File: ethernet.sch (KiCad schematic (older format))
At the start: 49 parts, among them U6 KSZ9031RNXCA, Y1 ABM8G-25.000MHZ-18-D2Y-T

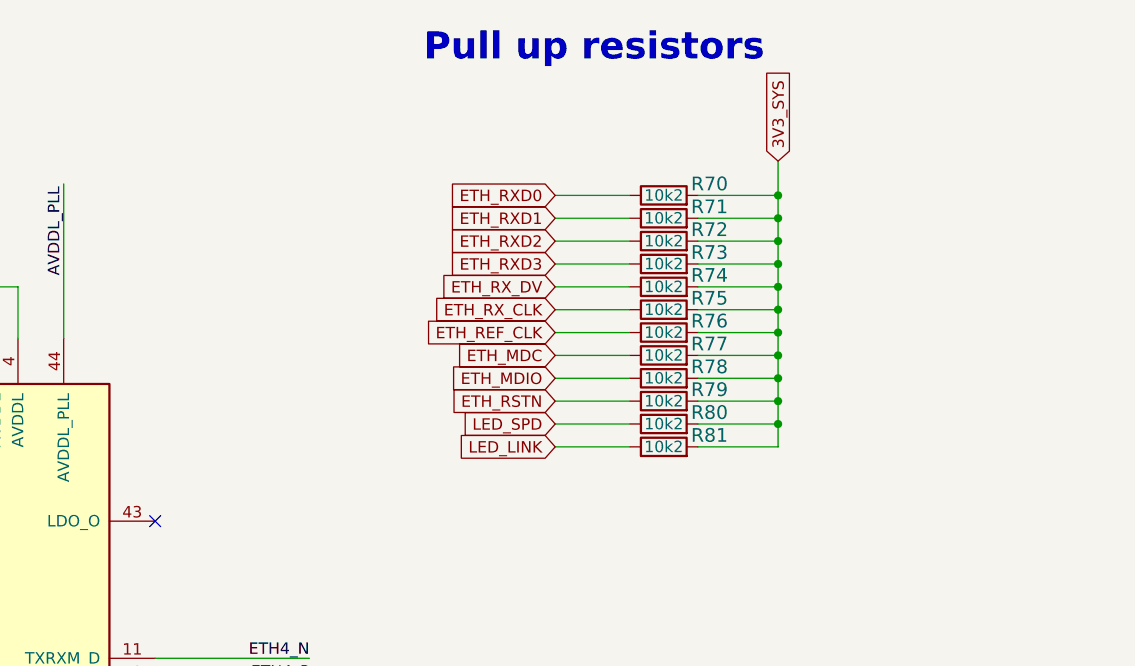
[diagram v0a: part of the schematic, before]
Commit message: Add bootstrap pull down resistors
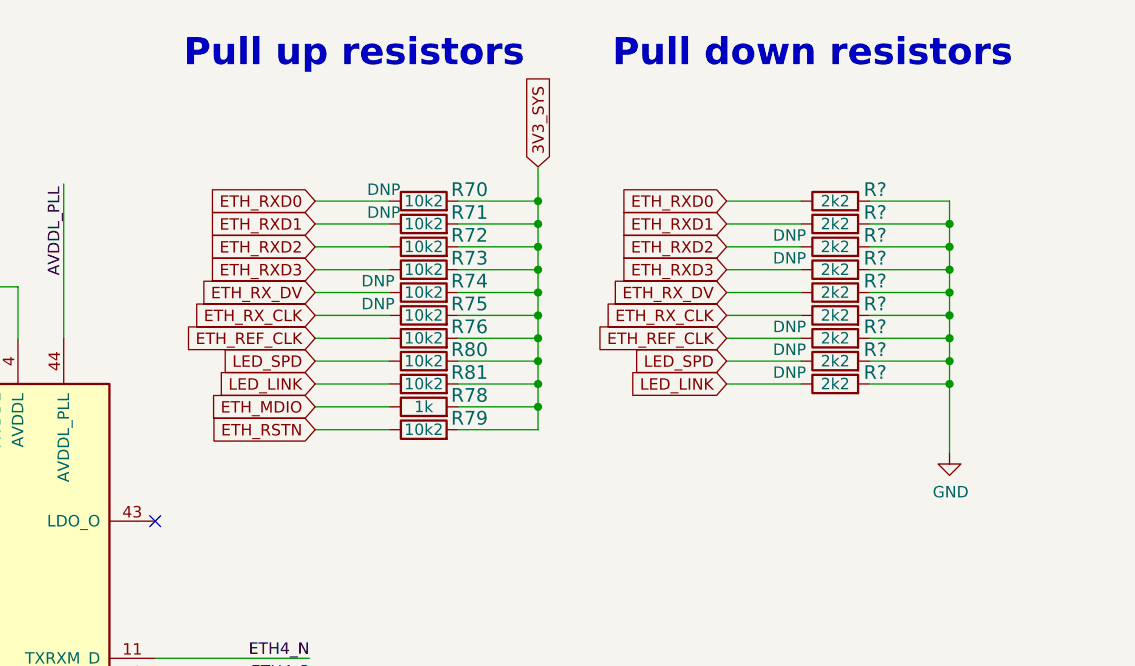
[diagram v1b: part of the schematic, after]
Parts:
- removed R77, R78: R_10k2_0402, lpddr4-test-board-footprints:0402-res, symbol lpddr4-test-board:R_10k2_0402
- added R78: R_1k_0402, antmicro-footprints:0402-res, symbol antmicroResistors0402:R_1k_0402
- added R? (x9): R_2k2_0402, antmicro-footprints:0402-res, symbol antmicroResistors0402:R_2k2_0402
- R70, R71, R74, R75: DNP (none) -> DNP
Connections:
- net 3V3_SYS: now also R78.2
- net ETH_MDIO: now also R78.1
- net ETH_REF_CLK: now also R?.1
- net ETH_RXD0: now also R?.1
- net ETH_RXD1: now also R?.1
- net ETH_RXD2: now also R?.1
- net ETH_RXD3: now also R?.1
- net ETH_RX_CLK: now also R?.1
- net ETH_RX_DV: now also R?.1
- net GND: now also R?.2, R?.2, R?.2, R?.2, R?.2, R?.2, R?.2, R?.2, R?.2
- net LED_LINK: now also R?.1
- net LED_SPD: now also R?.1
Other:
- note added: "Pull down resistors"
- moved on the sheet: R70, R71, R72, R73, R74, R75, R76, R79, R80, R81

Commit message: Bump release to 1.0.5
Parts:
- gave numbers to parts that had none: 9
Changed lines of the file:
@@
 	15300 2050 15650 2050
 $Comp
-L antmicroResistors0402:R_2k2_0402 R?
+L antmicroResistors0402:R_2k2_0402 R77
 U 1 1 6075D996
 P 15150 1750
-F 0 "R?" H 15325 1800 60  0000 C CNN
+F 0 "R77" H 15325 1800 60  0000 C CNN
 F 1 "R_2k2_0402" H 15150 1600 60  0001 C CNN
 F 2 "antmicro-footprints:0402-res" H 15350 1950 60  0001 L CNN
@@
 $EndComp
 $Comp
-L antmicroResistors0402:R_2k2_0402 R?
+L antmicroResistors0402:R_2k2_0402 R89
 U 1 1 60761864
 P 15150 1850
-F 0 "R?" H 15325 1900 60  0000 C CNN
+F 0 "R89" H 15325 1900 60  0000 C CNN
 F 1 "R_2k2_0402" H 15150 1700 60  0001 C CNN
 F 2 "antmicro-footprints:0402-res" H 15350 2050 60  0001 L CNN
@@
 $EndComp
 $Comp
-L antmicroResistors0402:R_2k2_0402 R?
+L antmicroResistors0402:R_2k2_0402 R90
 U 1 1 60761EC5
 P 15150 1950
-F 0 "R?" H 15325 2000 60  0000 C CNN
+F 0 "R90" H 15325 2000 60  0000 C CNN
 F 1 "R_2k2_0402" H 15150 1800 60  0001 C CNN
 F 2 "antmicro-footprints:0402-res" H 15350 2150 60  0001 L CNN
@@
 $EndComp
 $Comp
-L antmicroResistors0402:R_2k2_0402 R?
+L antmicroResistors0402:R_2k2_0402 R91
 U 1 1 607623D6
 P 15150 2050
-F 0 "R?" H 15325 2100 60  0000 C CNN
+F 0 "R91" H 15325 2100 60  0000 C CNN
 F 1 "R_2k2_0402" H 15150 1900 60  0001 C CNN
 F 2 "antmicro-footprints:0402-res" H 15350 2250 60  0001 L CNN
@@
 $EndComp
 $Comp
-L antmicroResistors0402:R_2k2_0402 R?
+L antmicroResistors0402:R_2k2_0402 R92
 U 1 1 6076538B
 P 15150 2150
-F 0 "R?" H 15325 2200 60  0000 C CNN
+F 0 "R92" H 15325 2200 60  0000 C CNN
 F 1 "R_2k2_0402" H 15150 2000 60  0001 C CNN
 F 2 "antmicro-footprints:0402-res" H 15350 2350 60  0001 L CNN
@@
 $EndComp
 $Comp
-L antmicroResistors0402:R_2k2_0402 R?
+L antmicroResistors0402:R_2k2_0402 R93
 U 1 1 607655D6
 P 15150 2250
-F 0 "R?" H 15325 2300 60  0000 C CNN
+F 0 "R93" H 15325 2300 60  0000 C CNN
 F 1 "R_2k2_0402" H 15150 2100 60  0001 C CNN
 F 2 "antmicro-footprints:0402-res" H 15350 2450 60  0001 L CNN
@@
 $EndComp
 $Comp
-L antmicroResistors0402:R_2k2_0402 R?
+L antmicroResistors0402:R_2k2_0402 R95
 U 1 1 6077DB28
 P 15150 2450
-F 0 "R?" H 15325 2500 60  0000 C CNN
+F 0 "R95" H 15325 2500 60  0000 C CNN
 F 1 "R_2k2_0402" H 15150 2300 60  0001 C CNN
 F 2 "antmicro-footprints:0402-res" H 15350 2650 60  0001 L CNN
@@
 $EndComp
 $Comp
-L antmicroResistors0402:R_2k2_0402 R?
+L antmicroResistors0402:R_2k2_0402 R96
 U 1 1 6077E011
 P 15150 2550
-F 0 "R?" H 15325 2600 60  0000 C CNN
+F 0 "R96" H 15325 2600 60  0000 C CNN
 F 1 "R_2k2_0402" H 15150 2400 60  0001 C CNN
 F 2 "antmicro-footprints:0402-res" H 15350 2750 60  0001 L CNN
@@
 	15650 2550 15650 2850
 $Comp
-L lpddr4-test-board:GND #PWR?
+L lpddr4-test-board:GND #PWR0129
 U 1 1 607C5C08
 P 15650 2850
-F 0 "#PWR?" H 15650 2600 50  0001 C CNN
+F 0 "#PWR0129" H 15650 2600 50  0001 C CNN
 F 1 "GND" H 15655 2677 50  0000 C CNN
 F 2 "" H 15650 2850 50  0001 C CNN
@@
 $EndComp
 $Comp
-L antmicroResistors0402:R_2k2_0402 R?
+L antmicroResistors0402:R_2k2_0402 R94
 U 1 1 607AC011
 P 15150 2350
-F 0 "R?" H 15325 2400 60  0000 C CNN
+F 0 "R94" H 15325 2400 60  0000 C CNN
 F 1 "R_2k2_0402" H 15150 2200 60  0001 C CNN
 F 2 "antmicro-footprints:0402-res" H 15350 2550 60  0001 L CNN

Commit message: Update component libraries
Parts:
- C122, C126, C130: footprint antmicro-footprints:0402-cap -> lpddr4-test-board-footprints:0402-cap; symbol antmicroCapacitors0402:C_470n_0402 -> lpddr4-test-board:C_470n_0402
- C135, C138, C141, C142: footprint antmicro-footprints:0402-cap -> lpddr4-test-board-footprints:0402-cap; symbol antmicroCapacitors0402:C_10n_0402 -> lpddr4-test-board:C_10n_0402
- C140: footprint antmicro-footprints:0402-cap -> lpddr4-test-board-footprints:0402-cap; symbol antmicroCapacitors0402:C_4u7_0402 -> lpddr4-test-board:C_4u7_0402
- C147, C148: footprint antmicro-footprints:0402-cap -> lpddr4-test-board-footprints:0402-cap; symbol antmicroCapacitors0402:C_22p_0402 -> lpddr4-test-board:C_22p_0402
- FB1, FB2, FB3, FB7: footprint antmicro-footprints:0603-res -> lpddr4-test-board-footprints:0603-res; symbol antmicroFerriteBeadsandChips:BLM18PG121SN1D -> lpddr4-test-board:BLM18PG121SN1D
- J?1: footprint antmicro-footprints:7499111121A -> lpddr4-test-board-footprints:7499111121A; symbol antmicroModularConnectorsJacksWithMagnetics:WE-RJ45_7499111121A -> lpddr4-test-board:WE-RJ45_7499111121A
- R68: footprint antmicro-footprints:0402-res -> lpddr4-test-board-footprints:0402-res; symbol antmicroResistors0402:R_12k1_0402 -> lpddr4-test-board:R_12k1_0402
- R69: footprint antmicro-footprints:0402-res -> lpddr4-test-board-footprints:0402-res; symbol antmicroResistors0402:R_1M8_0402 -> lpddr4-test-board:R_1M8_0402
- R77, R89, R90, R91, R92, R93, R94, R95, R96: footprint antmicro-footprints:0402-res -> lpddr4-test-board-footprints:0402-res; symbol antmicroResistors0402:R_2k2_0402 -> lpddr4-test-board:R_2k2_0402
- R78: footprint antmicro-footprints:0402-res -> lpddr4-test-board-footprints:0402-res; symbol antmicroResistors0402:R_1k_0402 -> lpddr4-test-board:R_1k_0402
- U6: footprint antmicro-footprints:QFN-48-Microchip-QFN77-48LD-PL-2 -> lpddr4-test-board-footprints:QFN-48-Microchip-QFN77-48LD-PL-2; symbol antmicroInterfaceControllers:KSZ9031RNXCA -> lpddr4-test-board:KSZ9031RNXCA
